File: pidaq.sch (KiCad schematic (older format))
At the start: 35 parts, among them J1 Screw_Terminal_01x08, J2 Screw_Terminal_01x08, J3 Screw_Terminal_01x10, J4 Screw_Terminal_01x10, J5 Conn_01x02_Male, J6 Conn_01x08_Female, U1 LTC2984CLX-PBF, U2 LTC2418IGN-PBF

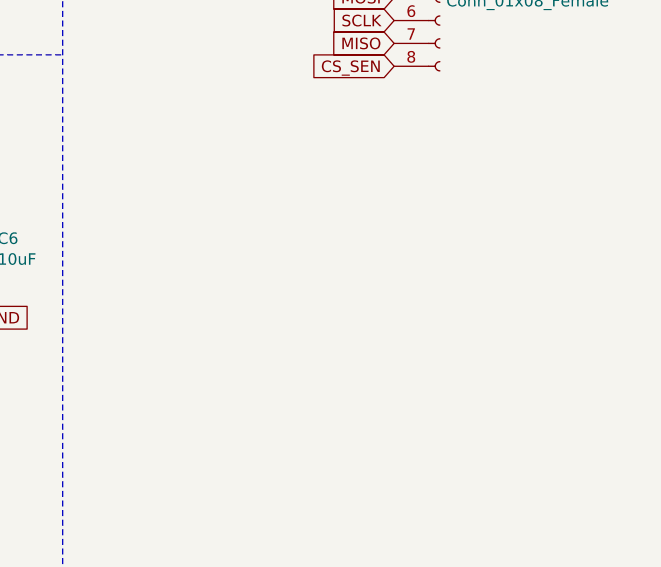
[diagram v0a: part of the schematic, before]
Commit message: finished silkscreen
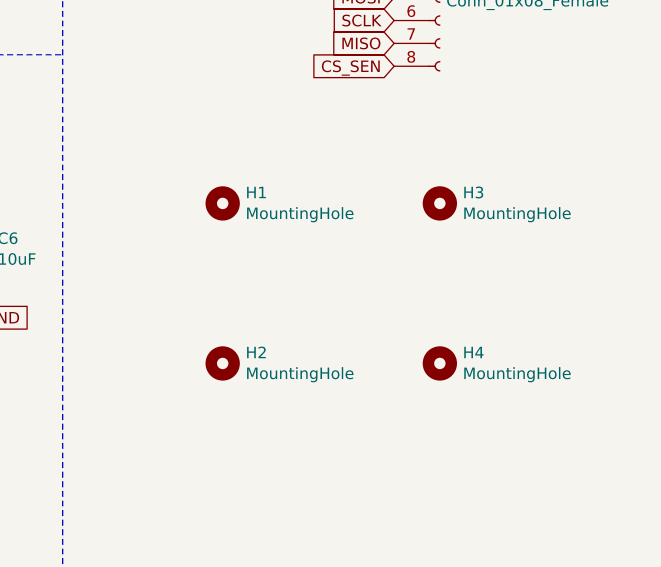
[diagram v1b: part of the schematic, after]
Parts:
- added H1, H2, H3, H4: MountingHole, MountingHole:MountingHole_3.2mm_M3, symbol Mechanical:MountingHole
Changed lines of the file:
@@
 	0    -1   -1   0
 $EndComp
+$Comp
+L Mechanical:MountingHole H1
+U 1 1 5ED3CDC2
+P 6600 3450
+F 0 "H1" H 6700 3496 50  0000 L CNN
+F 1 "MountingHole" H 6700 3405 50  0000 L CNN
+F 2 "MountingHole:MountingHole_3.2mm_M3" H 6600 3450 50  0001 C CNN
+F 3 "~" H 6600 3450 50  0001 C CNN
+	1    6600 3450
+	1    0    0    -1
+$EndComp
+$Comp
+L Mechanical:MountingHole H3
+U 1 1 5ED3DEFD
+P 7550 3450
+F 0 "H3" H 7650 3496 50  0000 L CNN
+F 1 "MountingHole" H 7650 3405 50  0000 L CNN
+F 2 "MountingHole:MountingHole_3.2mm_M3" H 7550 3450 50  0001 C CNN
+F 3 "~" H 7550 3450 50  0001 C CNN
+	1    7550 3450
+	1    0    0    -1
+$EndComp
+$Comp
+L Mechanical:MountingHole H2
+U 1 1 5ED3EC92
+P 6600 4150
+F 0 "H2" H 6700 4196 50  0000 L CNN
+F 1 "MountingHole" H 6700 4105 50  0000 L CNN
+F 2 "MountingHole:MountingHole_3.2mm_M3" H 6600 4150 50  0001 C CNN
+F 3 "~" H 6600 4150 50  0001 C CNN
+	1    6600 4150
+	1    0    0    -1
+$EndComp
+$Comp
+L Mechanical:MountingHole H4
+U 1 1 5ED3F653
+P 7550 4150
+F 0 "H4" H 7650 4196 50  0000 L CNN
+F 1 "MountingHole" H 7650 4105 50  0000 L CNN
+F 2 "MountingHole:MountingHole_3.2mm_M3" H 7550 4150 50  0001 C CNN
+F 3 "~" H 7550 4150 50  0001 C CNN
+	1    7550 4150
+	1    0    0    -1
+$EndComp
 $EndSCHEMATC

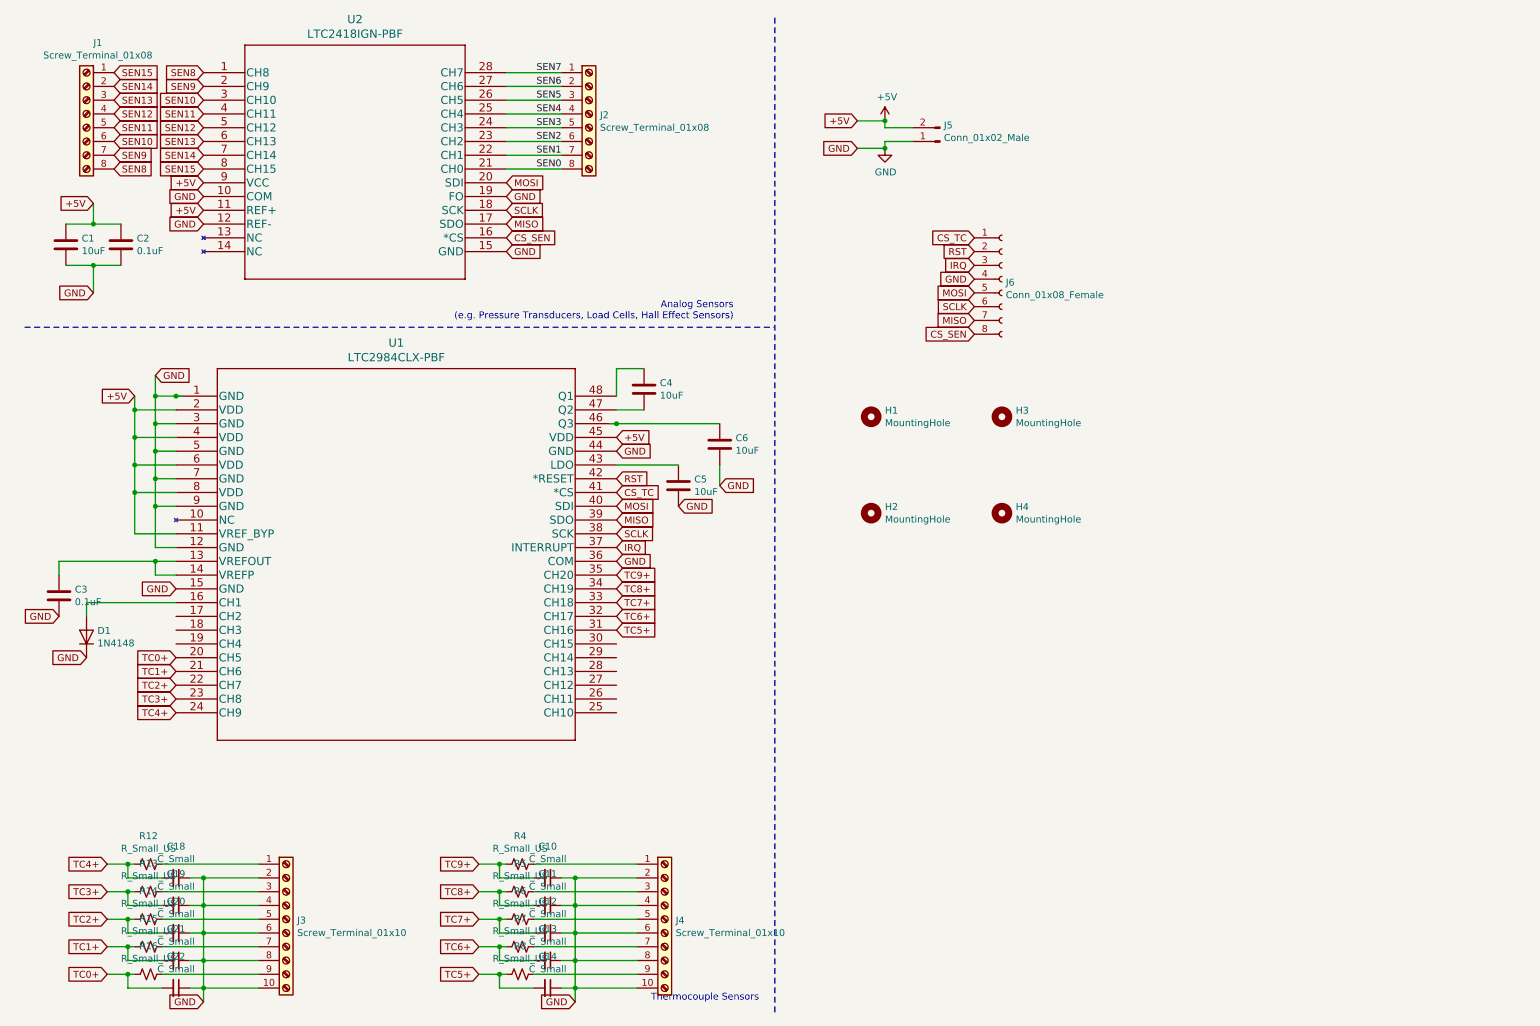
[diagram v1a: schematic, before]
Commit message: add html preview
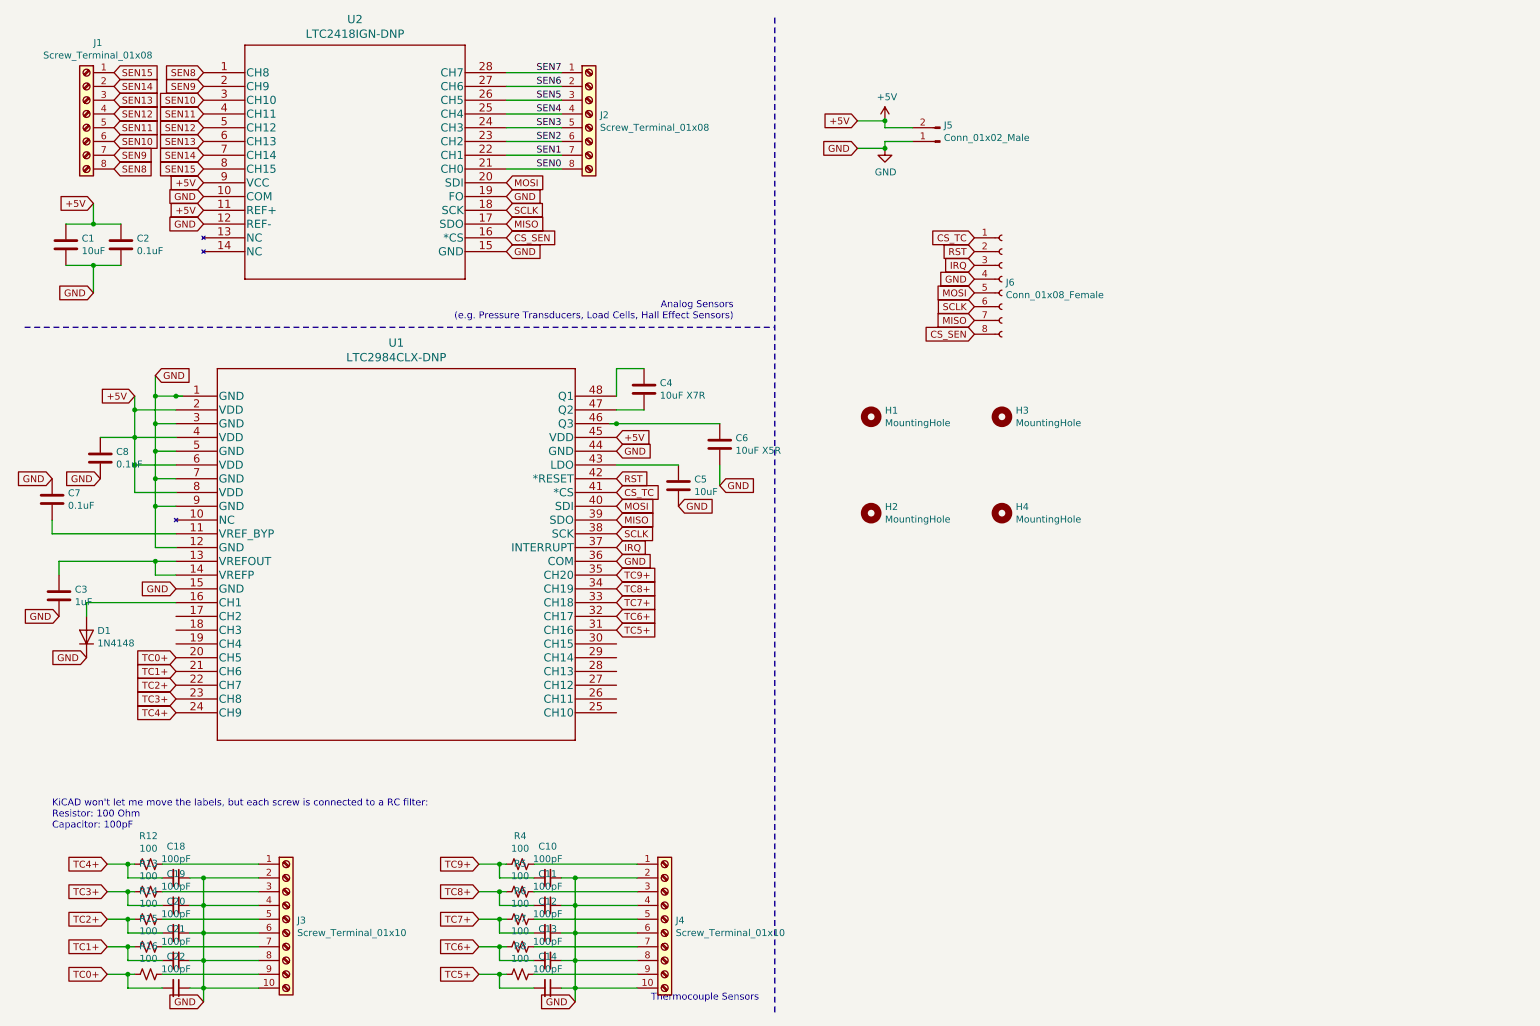
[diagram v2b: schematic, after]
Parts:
- added C7, C8: 0.1uF, Capacitor_SMD:C_0805_2012Metric_Pad1.15x1.40mm_HandSolder, symbol Device:C
- C10, C11, C12, C13, C14, C18, C19, C20, C21, C22: value C_Small -> 100pF
- C3: value 0.1uF -> 1uF
- C4: value 10uF -> 10uF X7R
- C6: value 10uF -> 10uF X5R
- R12, R13, R14, R15, R16, R4, R5, R6, R7, R8: value R_Small_US -> 100
- U1: value LTC2984CLX-PBF -> LTC2984CLX-DNP
- U2: value LTC2418IGN-PBF -> LTC2418IGN-DNP
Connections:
- net +5V: now also C8.1; no longer U1.11 (VREF_BYP)
- net GND: now also C7.1, C8.2
- new net: C7.2, U1.11 (VREF_BYP)
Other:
- note added: "KiCAD won't let me move the labels, but each screw is connected to a RC filter:\nResistor: 100 Ohm\nCapacitor: 100pF"
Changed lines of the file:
@@
 AR Path="/5ED56214/5EDBB969" Ref="U?"  Part="1"
 F 0 "U2" H 2850 1337 60  0000 C CNN
-F 1 "LTC2418IGN-PBF" H 2850 1231 60  0000 C CNN
+F 1 "LTC2418IGN-DNP" H 2850 1231 60  0000 C CNN
 F 2 "proj_footprints:LTC2418IGN-PBF" H 2850 1190 60  0001 C CNN
 F 3 "" H 1750 950 60  0000 C CNN
@@
 P 4950 3250
 F 0 "C4" H 5065 3296 50  0000 L CNN
-F 1 "10uF" H 5065 3205 50  0000 L CNN
+F 1 "10uF X7R" H 5065 3205 50  0000 L CNN
 F 2 "Capacitor_SMD:C_0805_2012Metric_Pad1.15x1.40mm_HandSolder" H 4988 3100 50  0001 C CNN
 F 3 "~" H 4950 3250 50  0001 C CNN
@@
 P 5500 3650
 F 0 "C6" H 5615 3696 50  0000 L CNN
-F 1 "10uF" H 5615 3605 50  0000 L CNN
+F 1 "10uF X5R" H 5615 3605 50  0000 L CNN
 F 2 "Capacitor_SMD:C_0805_2012Metric_Pad1.15x1.40mm_HandSolder" H 5538 3500 50  0001 C CNN
 F 3 "~" H 5500 3650 50  0001 C CNN
@@
 +5V
 Wire Wire Line
-	1250 4000 1250 4300
-Wire Wire Line
-	1250 4300 1550 4300
-Connection ~ 1250 4000
-Wire Wire Line
 	1400 4100 1400 4400
 Wire Wire Line
@@
 P 700 4750
 F 0 "C3" H 815 4796 50  0000 L CNN
-F 1 "0.1uF" H 815 4705 50  0000 L CNN
+F 1 "1uF" H 815 4705 50  0000 L CNN
 F 2 "Capacitor_SMD:C_0805_2012Metric_Pad1.15x1.40mm_HandSolder" H 738 4600 50  0001 C CNN
 F 3 "~" H 700 4750 50  0001 C CNN
@@
 P 1550 3300
 F 0 "U1" H 3150 3687 60  0000 C CNN
-F 1 "LTC2984CLX-PBF" H 3150 3581 60  0000 C CNN
+F 1 "LTC2984CLX-DNP" H 3150 3581 60  0000 C CNN
 F 2 "proj_footprints:LTC2984CLX-PBF" H 3150 3540 60  0001 C CNN
 F 3 "" H 1550 3300 60  0000 C CNN
@@
 P 4250 7600
 F 0 "C14" V 4021 7600 50  0000 C CNN
-F 1 "C_Small" V 4112 7600 50  0000 C CNN
+F 1 "100pF" V 4112 7600 50  0000 C CNN
 F 2 "Capacitor_SMD:C_0805_2012Metric_Pad1.15x1.40mm_HandSolder" H 4250 7600 50  0001 C CNN
 F 3 "~" H 4250 7600 50  0001 C CNN
@@
 P 4050 7500
 F 0 "R8" V 3845 7500 50  0000 C CNN
-F 1 "R_Small_US" V 3936 7500 50  0000 C CNN
+F 1 "100" V 3936 7500 50  0000 C CNN
 F 2 "Resistor_SMD:R_0805_2012Metric_Pad1.15x1.40mm_HandSolder" H 4050 7500 50  0001 C CNN
 F 3 "~" H 4050 7500 50  0001 C CNN
@@
 P 4250 7400
 F 0 "C13" V 4021 7400 50  0000 C CNN
-F 1 "C_Small" V 4112 7400 50  0000 C CNN
+F 1 "100pF" V 4112 7400 50  0000 C CNN
 F 2 "Capacitor_SMD:C_0805_2012Metric_Pad1.15x1.40mm_HandSolder" H 4250 7400 50  0001 C CNN
 F 3 "~" H 4250 7400 50  0001 C CNN
@@
 P 4050 7300
 F 0 "R7" V 3845 7300 50  0000 C CNN
-F 1 "R_Small_US" V 3936 7300 50  0000 C CNN
+F 1 "100" V 3936 7300 50  0000 C CNN
 F 2 "Resistor_SMD:R_0805_2012Metric_Pad1.15x1.40mm_HandSolder" H 4050 7300 50  0001 C CNN
 F 3 "~" H 4050 7300 50  0001 C CNN
@@
 P 4250 7200
 F 0 "C12" V 4021 7200 50  0000 C CNN
-F 1 "C_Small" V 4112 7200 50  0000 C CNN
+F 1 "100pF" V 4112 7200 50  0000 C CNN
 F 2 "Capacitor_SMD:C_0805_2012Metric_Pad1.15x1.40mm_HandSolder" H 4250 7200 50  0001 C CNN
 F 3 "~" H 4250 7200 50  0001 C CNN
@@
 P 4050 7100
 F 0 "R6" V 3845 7100 50  0000 C CNN
-F 1 "R_Small_US" V 3936 7100 50  0000 C CNN
+F 1 "100" V 3936 7100 50  0000 C CNN
 F 2 "Resistor_SMD:R_0805_2012Metric_Pad1.15x1.40mm_HandSolder" H 4050 7100 50  0001 C CNN
 F 3 "~" H 4050 7100 50  0001 C CNN
@@
 P 4250 7000
 F 0 "C11" V 4021 7000 50  0000 C CNN
-F 1 "C_Small" V 4112 7000 50  0000 C CNN
+F 1 "100pF" V 4112 7000 50  0000 C CNN
 F 2 "Capacitor_SMD:C_0805_2012Metric_Pad1.15x1.40mm_HandSolder" H 4250 7000 50  0001 C CNN
 F 3 "~" H 4250 7000 50  0001 C CNN
@@
 P 4050 6900
 F 0 "R5" V 3845 6900 50  0000 C CNN
-F 1 "R_Small_US" V 3936 6900 50  0000 C CNN
+F 1 "100" V 3936 6900 50  0000 C CNN
 F 2 "Resistor_SMD:R_0805_2012Metric_Pad1.15x1.40mm_HandSolder" H 4050 6900 50  0001 C CNN
 F 3 "~" H 4050 6900 50  0001 C CNN
@@
 P 4250 6800
 F 0 "C10" V 4021 6800 50  0000 C CNN
-F 1 "C_Small" V 4112 6800 50  0000 C CNN
+F 1 "100pF" V 4112 6800 50  0000 C CNN
 F 2 "Capacitor_SMD:C_0805_2012Metric_Pad1.15x1.40mm_HandSolder" H 4250 6800 50  0001 C CNN
 F 3 "~" H 4250 6800 50  0001 C CNN
@@
 P 4050 6700
 F 0 "R4" V 3845 6700 50  0000 C CNN
-F 1 "R_Small_US" V 3936 6700 50  0000 C CNN
+F 1 "100" V 3936 6700 50  0000 C CNN
 F 2 "Resistor_SMD:R_0805_2012Metric_Pad1.15x1.40mm_HandSolder" H 4050 6700 50  0001 C CNN
 F 3 "~" H 4050 6700 50  0001 C CNN
@@
 P 1550 7600
 F 0 "C22" V 1321 7600 50  0000 C CNN
-F 1 "C_Small" V 1412 7600 50  0000 C CNN
+F 1 "100pF" V 1412 7600 50  0000 C CNN
 F 2 "Capacitor_SMD:C_0805_2012Metric_Pad1.15x1.40mm_HandSolder" H 1550 7600 50  0001 C CNN
 F 3 "~" H 1550 7600 50  0001 C CNN
@@
 P 1350 7500
 F 0 "R16" V 1145 7500 50  0000 C CNN
-F 1 "R_Small_US" V 1236 7500 50  0000 C CNN
+F 1 "100" V 1236 7500 50  0000 C CNN
 F 2 "Resistor_SMD:R_0805_2012Metric_Pad1.15x1.40mm_HandSolder" H 1350 7500 50  0001 C CNN
 F 3 "~" H 1350 7500 50  0001 C CNN
@@
 P 1550 7400
 F 0 "C21" V 1321 7400 50  0000 C CNN
-F 1 "C_Small" V 1412 7400 50  0000 C CNN
+F 1 "100pF" V 1412 7400 50  0000 C CNN
 F 2 "Capacitor_SMD:C_0805_2012Metric_Pad1.15x1.40mm_HandSolder" H 1550 7400 50  0001 C CNN
 F 3 "~" H 1550 7400 50  0001 C CNN
@@
 P 1350 7300
 F 0 "R15" V 1145 7300 50  0000 C CNN
-F 1 "R_Small_US" V 1236 7300 50  0000 C CNN
+F 1 "100" V 1236 7300 50  0000 C CNN
 F 2 "Resistor_SMD:R_0805_2012Metric_Pad1.15x1.40mm_HandSolder" H 1350 7300 50  0001 C CNN
 F 3 "~" H 1350 7300 50  0001 C CNN
@@
 P 1550 7200
 F 0 "C20" V 1321 7200 50  0000 C CNN
-F 1 "C_Small" V 1412 7200 50  0000 C CNN
+F 1 "100pF" V 1412 7200 50  0000 C CNN
 F 2 "Capacitor_SMD:C_0805_2012Metric_Pad1.15x1.40mm_HandSolder" H 1550 7200 50  0001 C CNN
 F 3 "~" H 1550 7200 50  0001 C CNN
@@
 P 1350 7100
 F 0 "R14" V 1145 7100 50  0000 C CNN
-F 1 "R_Small_US" V 1236 7100 50  0000 C CNN
+F 1 "100" V 1236 7100 50  0000 C CNN
 F 2 "Resistor_SMD:R_0805_2012Metric_Pad1.15x1.40mm_HandSolder" H 1350 7100 50  0001 C CNN
 F 3 "~" H 1350 7100 50  0001 C CNN
@@
 P 1550 7000
 F 0 "C19" V 1321 7000 50  0000 C CNN
-F 1 "C_Small" V 1412 7000 50  0000 C CNN
+F 1 "100pF" V 1412 7000 50  0000 C CNN
 F 2 "Capacitor_SMD:C_0805_2012Metric_Pad1.15x1.40mm_HandSolder" H 1550 7000 50  0001 C CNN
 F 3 "~" H 1550 7000 50  0001 C CNN
@@
 P 1350 6900
 F 0 "R13" V 1145 6900 50  0000 C CNN
-F 1 "R_Small_US" V 1236 6900 50  0000 C CNN
+F 1 "100" V 1236 6900 50  0000 C CNN
 F 2 "Resistor_SMD:R_0805_2012Metric_Pad1.15x1.40mm_HandSolder" H 1350 6900 50  0001 C CNN
 F 3 "~" H 1350 6900 50  0001 C CNN
@@
 P 1550 6800
 F 0 "C18" V 1321 6800 50  0000 C CNN
-F 1 "C_Small" V 1412 6800 50  0000 C CNN
+F 1 "100pF" V 1412 6800 50  0000 C CNN
 F 2 "Capacitor_SMD:C_0805_2012Metric_Pad1.15x1.40mm_HandSolder" H 1550 6800 50  0001 C CNN
 F 3 "~" H 1550 6800 50  0001 C CNN
@@
 P 1350 6700
 F 0 "R12" V 1145 6700 50  0000 C CNN
-F 1 "R_Small_US" V 1236 6700 50  0000 C CNN
+F 1 "100" V 1236 6700 50  0000 C CNN
 F 2 "Resistor_SMD:R_0805_2012Metric_Pad1.15x1.40mm_HandSolder" H 1350 6700 50  0001 C CNN
 F 3 "~" H 1350 6700 50  0001 C CNN
@@
 	1    0    0    -1
 $EndComp
+Text Notes 650  6450 0    50   ~ 0
+KiCAD won't let me move the labels, but each screw is connected to a RC filter:\nResistor: 100 Ohm\nCapacitor: 100pF
+$Comp
+L Device:C C7
+U 1 1 5ED3F1A8
+P 650 4050
+F 0 "C7" H 765 4096 50  0000 L CNN
+F 1 "0.1uF" H 765 4005 50  0000 L CNN
+F 2 "Capacitor_SMD:C_0805_2012Metric_Pad1.15x1.40mm_HandSolder" H 688 3900 50  0001 C CNN
+F 3 "~" H 650 4050 50  0001 C CNN
+	1    650  4050
+	1    0    0    -1
+$EndComp
+$Comp
+L Device:C C8
+U 1 1 5ED54EA2
+P 1000 3750
+F 0 "C8" H 1115 3796 50  0000 L CNN
+F 1 "0.1uF" H 1115 3705 50  0000 L CNN
+F 2 "Capacitor_SMD:C_0805_2012Metric_Pad1.15x1.40mm_HandSolder" H 1038 3600 50  0001 C CNN
+F 3 "~" H 1000 3750 50  0001 C CNN
+	1    1000 3750
+	1    0    0    -1
+$EndComp
+Wire Wire Line
+	1550 4300 650  4300
+Wire Wire Line
+	650  4300 650  4200
+Wire Wire Line
+	1250 3600 1000 3600
+Text GLabel 650  3900 0    50   Input ~ 0
+GND
+Text GLabel 1000 3900 0    50   Input ~ 0
+GND
 $EndSCHEMATC
